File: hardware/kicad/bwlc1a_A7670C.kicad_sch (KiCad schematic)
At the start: 58 parts, among them J3 SIM_Card, J5 USB_BOOT, Q1 NPN, Q2 NPN, Q5 NPN, Q6 NPN, U5 MIC29302WU

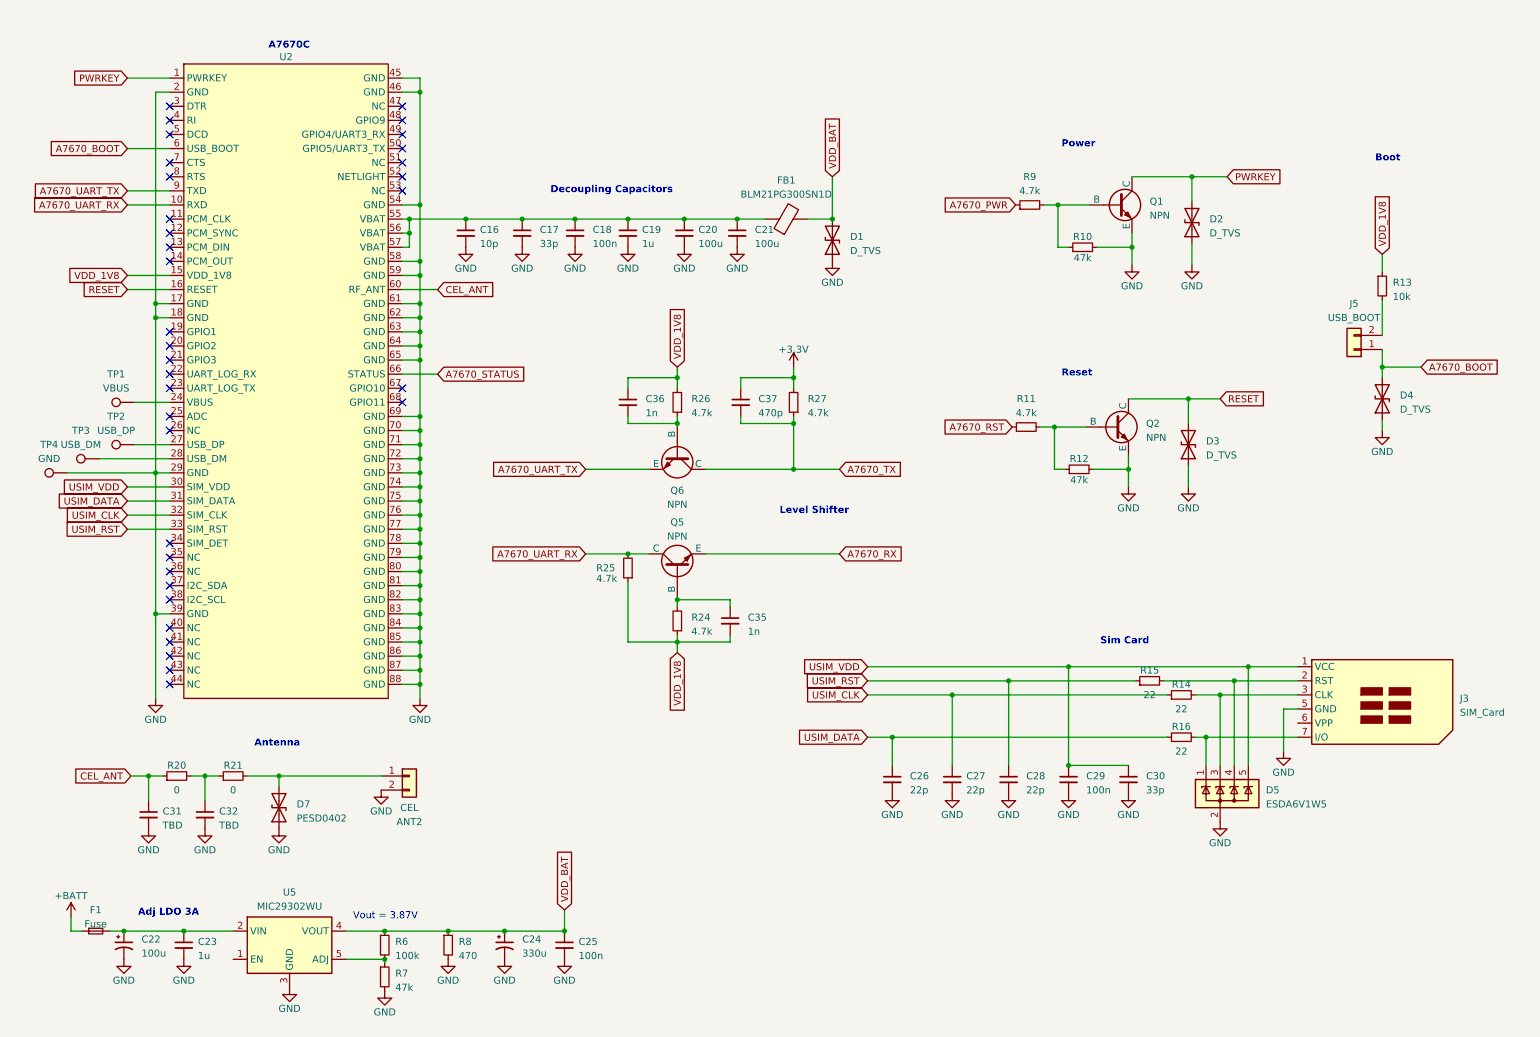
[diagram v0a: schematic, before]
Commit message: Finish Sch, start Layouting
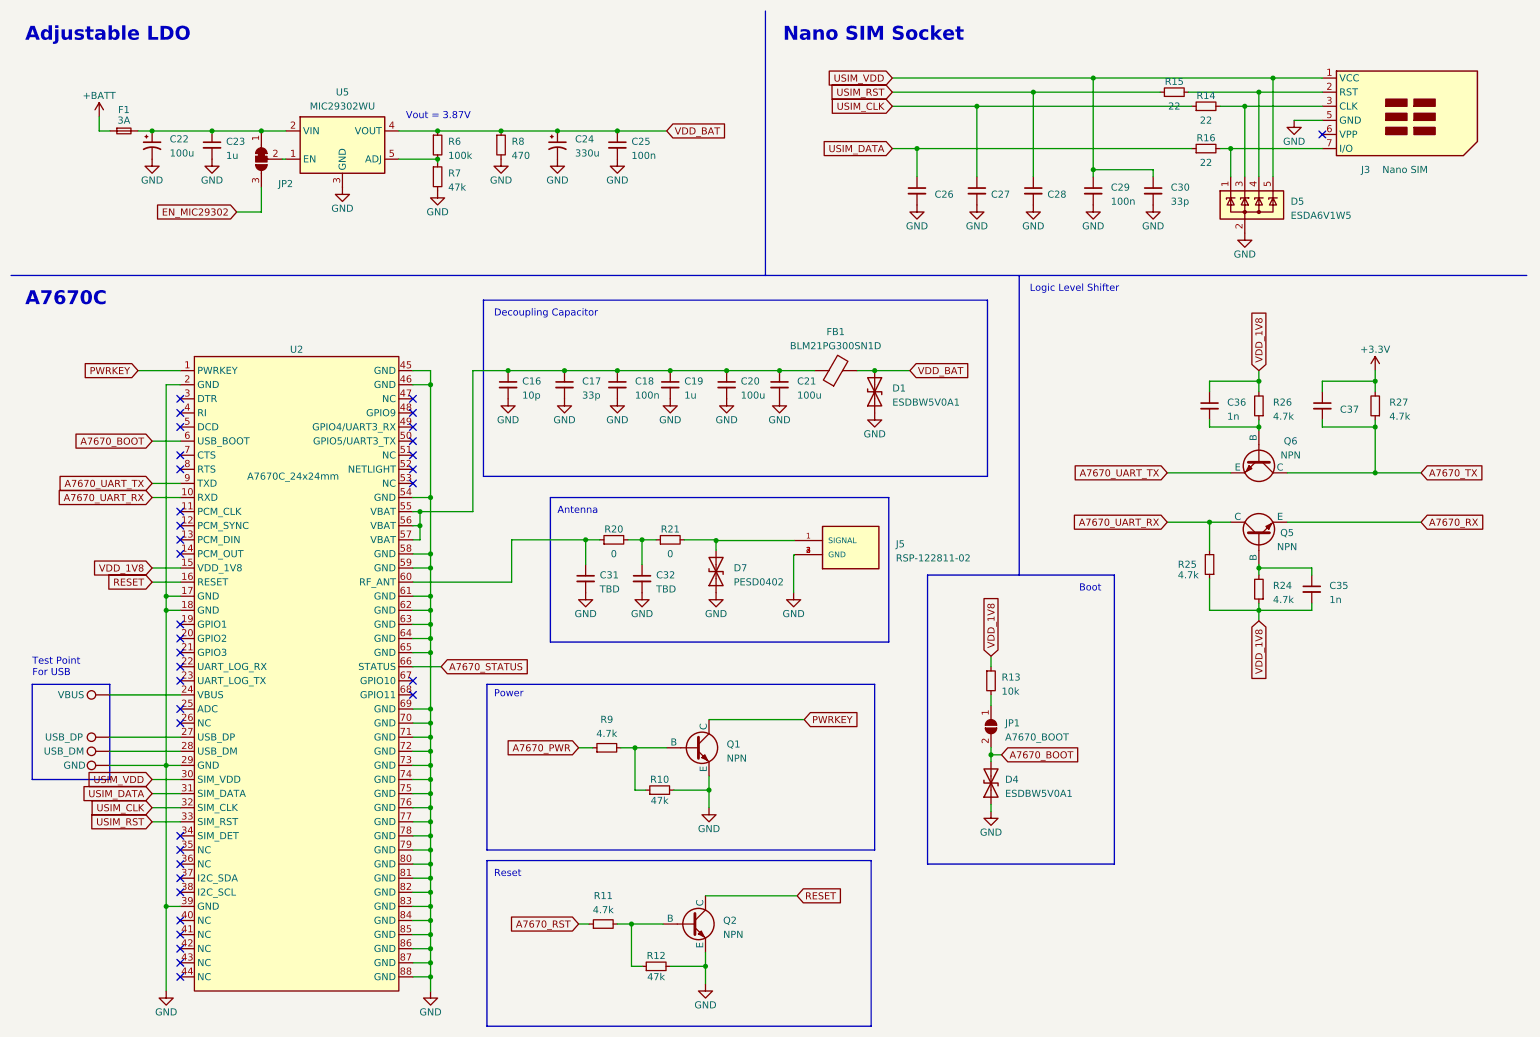
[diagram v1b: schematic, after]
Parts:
- removed ANT2: CEL, symbol Connector_Generic:Conn_01x02
- removed D2, D3: D_TVS, symbol Device:D_TVS
- removed J5: USB_BOOT, symbol Connector_Generic:Conn_01x02
- added J5: RSP-122811-02, SAMTEC_RSP-122811-02:SAMTEC_RSP-122811-02, symbol RSP-122811-02:RSP-122811-02
- added JP1: A7670_BOOT, Jumper:SolderJumper-2_P1.3mm_Open_RoundedPad1.0x1.5mm, symbol Jumper:SolderJumper_2_Open
- added JP2: EN_MIC29302, Jumper:SolderJumper-3_P1.3mm_Bridged2Bar12_RoundedPad1.0x1.5mm, symbol Jumper:SolderJumper_3_Bridged12
- C16, C17, C18, C19, C20, C21, C23, C25, C29, C30, C31, C32, C35, C36, D7: footprint (none) -> Capacitor_SMD:C_0402_1005Metric
- C22: footprint (none) -> Capacitor_SMD:CP_Elec_6.3x5.4
- C24: footprint (none) -> Capacitor_SMD:CP_Elec_8x10.5
- C26, C27, C28: value 22p -> 22p (N.C.); footprint (none) -> Capacitor_SMD:C_0402_1005Metric
- C37: value 470p -> 470p (N.C); footprint (none) -> Capacitor_SMD:C_0402_1005Metric
- D1, D4: value D_TVS -> ESDBW5V0A1; footprint (none) -> Capacitor_SMD:C_0402_1005Metric
- F1: value Fuse -> 3A; footprint (none) -> Fuse:Fuse_1206_3216Metric
- FB1: footprint (none) -> Capacitor_SMD:C_0805_2012Metric
- J3: value SIM_Card -> Nano SIM; footprint (none) -> GCT_SIM8051-6-0-14-00-X-REVD:GCT_SIM8051-6-0-14-00-X-REVD; Field4 (none) -> C266889
- Q1, Q2, Q5, Q6: footprint (none) -> Package_TO_SOT_SMD:SOT-23
- R10, R11, R12, R13, R14, R15, R16, R20, R21, R24, R25, R26, R27, R6, R7, R8, R9: footprint (none) -> Resistor_SMD:R_0402_1005Metric
- TP1, TP2, TP3, TP4: footprint (none) -> TestPoint:TestPoint_Pad_D1.5mm
- U2: value ~ -> A7670C_24x24mm; footprint (none) -> Teapot:A7670C_24x24mm
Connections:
- net A7670_BOOT: now also JP1.2 (B)
- net GND: now also J5.2 (GND), J5.3 (GND), J5.4 (GND)
- net at D7.2 (A2), R21.2: now also J5.1 (SIGNAL)
- net at R13.2: now also JP1.1 (A)
- net at C22.1, C23.1, F1.2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: now also JP2.1 (A)
- net at U5.1 (EN): now also JP2.2 (C)
- net CEL_ANT: no longer names the net of C31.1, R20.1, U2.60 (RF_ANT)
- new net EN_MIC29302: JP2.3 (B)
- no-connect marks 35 -> 36
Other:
- note added: "Adjustable LDO"
- note added: "Decoupling Capacitor"
- note added: "Logic Level Shifter"
- note added: "Nano SIM Socket"
- note added: "Test Point For USB"
- note removed: "Adj LDO 3A"
- note removed: "Decoupling Capacitors"
- note removed: "Level Shifter"
- note removed: "Sim Card"
- moved on the sheet: C16, C17, C18, C19, C20, C21, C22, C23, C24, C25, C26, C27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

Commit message: Update on PCB Layout
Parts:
- added C36: 100n, Capacitor_SMD:C_0402_1005Metric, symbol Device:C_Small
- C20, C21, C23: footprint Capacitor_SMD:C_0402_1005Metric -> Capacitor_SMD:C_0603_1608Metric
- C25: footprint Capacitor_SMD:C_0402_1005Metric -> Capacitor_SMD:C_0805_2012Metric
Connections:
- net GND: now also C36.2
- net VDD_1V8: now also C36.1
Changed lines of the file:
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@@
   (junction (at 139.065 107.442) (diameter 0) (color 0 0 0 0)
   )
+  (junction (at 27.305 112.395) (diameter 0) (color 0 0 0 0)
+  )
   (junction (at 40.005 173.355) (diameter 0) (color 0 0 0 0)
   )
@@
     (stroke (width 0) (type default))
   )
-  (wire (pts (xy 37.465 112.395) (xy 42.545 112.395))
+  (wire (pts (xy 26.035 112.395) (xy 27.305 112.395))
     (stroke (width 0) (type default))
   )
@@
     (stroke (width 0) (type default))
   )
+  (wire (pts (xy 27.305 112.395) (xy 42.545 112.395))
+    (stroke (width 0) (type default))
+  )
   (wire (pts (xy 87.63 109.855) (xy 87.63 99.695))
     (stroke (width 0) (type default))
@@
     )
   )
-  (global_label "VDD_1V8" (shape input) (at 37.465 112.395 180) (fields_autoplaced)
+  (global_label "VDD_1V8" (shape input) (at 26.035 112.395 180) (fields_autoplaced)
     (effects (font (size 1.27 1.27)) (justify right))
-    (property "Intersheetrefs" "${INTERSHEET_REFS}" (at 26.4554 112.395 0)
+    (property "Intersheetrefs" "${INTERSHEET_REFS}" (at 15.0254 112.395 0)
       (effects (font (size 1.27 1.27)) (justify right) hide)
     )
@@
       (effects (font (size 1.27 1.27)) (justify left))
     )
-    (property "Footprint" "Capacitor_SMD:C_0402_1005Metric" (at 140.97 79.375 0)
+    (property "Footprint" "Capacitor_SMD:C_0603_1608Metric" (at 140.97 79.375 0)
       (effects (font (size 1.27 1.27)) hide)
     )
@@
       (effects (font (size 1.27 1.27)) (justify left))
     )
-    (property "Footprint" "Capacitor_SMD:C_0402_1005Metric" (at 48.26 36.195 0)
+    (property "Footprint" "Capacitor_SMD:C_0603_1608Metric" (at 48.26 36.195 0)
       (effects (font (size 1.27 1.27)) hide)
     )
@@
       (effects (font (size 1.27 1.27)) (justify left))
     )
-    (property "Footprint" "Capacitor_SMD:C_0402_1005Metric" (at 121.285 36.195 0)
+    (property "Footprint" "Capacitor_SMD:C_0805_2012Metric" (at 121.285 36.195 0)
       (effects (font (size 1.27 1.27)) hide)
     )
@@
       (effects (font (size 1.27 1.27)) (justify left))
     )
-    (property "Footprint" "Capacitor_SMD:C_0402_1005Metric" (at 150.495 79.375 0)
+    (property "Footprint" "Capacitor_SMD:C_0603_1608Metric" (at 150.495 79.375 0)
       (effects (font (size 1.27 1.27)) hide)
     )
@@
     )
   )
+  (symbol (lib_id "Device:C_Small") (at 27.305 114.935 0) (unit 1)
+    (in_bom yes) (on_board yes) (dnp no) (fields_autoplaced)
+    (property "Reference" "C36" (at 30.48 114.3063 0)
+      (effects (font (size 1.27 1.27)) (justify left))
+    )
+    (property "Value" "100n" (at 30.48 116.8463 0)
+      (effects (font (size 1.27 1.27)) (justify left))
+    )
+    (property "Footprint" "Capacitor_SMD:C_0402_1005Metric" (at 27.305 114.935 0)
+      (effects (font (size 1.27 1.27)) hide)
+    )
+    (property "Datasheet" "~" (at 27.305 114.935 0)
+      (effects (font (size 1.27 1.27)) hide)
+    )
+    (pin "1")
+    (pin "2")
+    (instances
+      (project "bwlc1a"
+        (path "/388039b1-99cc-430f-bd4a-010573fde798"
+          (reference "C36") (unit 1)
+        )
+        (path "/388039b1-99cc-430f-bd4a-010573fde798/d0b0fe7e-ffcb-4a20-b7b5-70f0caeaf6a1"
+          (reference "C38") (unit 1)
+        )
+      )
+    )
+  )
   (symbol (lib_id "power:GND") (at 115.57 116.84 0) (unit 1)
     (in_bom yes) (on_board yes) (dnp no)
@@
         )
       )
+    )
+  )
+  (symbol (lib_id "power:GND") (at 27.305 117.475 0) (unit 1)
+    (in_bom yes) (on_board yes) (dnp no)
+    (property "Reference" "#PWR063" (at 27.305 123.825 0)
+      (effects (font (size 1.27 1.27)) hide)
+    )
+    (property "Value" "GND" (at 27.305 121.285 0)
+      (effects (font (size 1.27 1.27)))
+    )
+    (property "Footprint" "" (at 27.305 117.475 0)
+      (effects (font (size 1.27 1.27)) hide)
+    )
+    (property "Datasheet" "" (at 27.305 117.475 0)
+      (effects (font (size 1.27 1.27)) hide)
+    )
+    (pin "1")
+    (instances
+      (project "bwlc1a"
+        (path "/388039b1-99cc-430f-bd4a-010573fde798"
+          (reference "#PWR063") (unit 1)
+        )
+        (path "/388039b1-99cc-430f-bd4a-010573fde798/d0b0fe7e-ffcb-4a20-b7b5-70f0caeaf6a1"
+          (reference "#PWR089") (unit 1)
+        )
+      )

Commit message: Update on routing
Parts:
- removed C26, C27, C28: 22p (N.C.), Capacitor_SMD:C_0402_1005Metric, symbol Device:C_Small
- removed C30: 33p, Capacitor_SMD:C_0402_1005Metric, symbol Device:C_Small
- C24: footprint Capacitor_SMD:CP_Elec_8x10.5 -> Capacitor_SMD:CP_Elec_6.3x7.7

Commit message: PCB Layout update + Silkscreen
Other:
- moved on the sheet: JP2
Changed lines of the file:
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@@
   (junction (at 88.9 38.735) (diameter 0) (color 0 0 0 0)
   )
+  (junction (at 57.785 33.655) (diameter 0) (color 0 0 0 0)
+  )
   (junction (at 87.63 155.575) (diameter 0) (color 0 0 0 0)
   )
@@
   )
   (junction (at 87.63 163.195) (diameter 0) (color 0 0 0 0)
-  )
-  (junction (at 57.15 33.655) (diameter 0) (color 0 0 0 0)
   )
   (junction (at 40.005 120.015) (diameter 0) (color 0 0 0 0)
@@
     (stroke (width 0) (type default))
   )
-  (wire (pts (xy 48.26 33.655) (xy 57.15 33.655))
-    (stroke (width 0) (type default))
-  )
   (wire (pts (xy 84.455 145.415) (xy 87.63 145.415))
     (stroke (width 0) (type default))
@@
     (stroke (width 0) (type default))
   )
+  (wire (pts (xy 57.785 48.26) (xy 49.53 48.26))
+    (stroke (width 0) (type default))
+  )
   (wire (pts (xy 87.63 153.035) (xy 87.63 150.495))
     (stroke (width 0) (type default))
@@
     (stroke (width 0) (type default))
   )
+  (wire (pts (xy 57.785 33.655) (xy 61.595 33.655))
+    (stroke (width 0) (type default))
+  )
   (wire (pts (xy 84.455 168.275) (xy 87.63 168.275))
     (stroke (width 0) (type default))
@@
     (stroke (width 0) (type default))
   )
-  (wire (pts (xy 57.15 48.26) (xy 57.15 43.815))
-    (stroke (width 0) (type default))
-  )
   (wire (pts (xy 37.465 89.535) (xy 42.545 89.535))
     (stroke (width 0) (type default))
@@
     (stroke (width 0) (type default))
   )
-  (wire (pts (xy 57.15 33.655) (xy 61.595 33.655))
+  (wire (pts (xy 48.26 33.655) (xy 57.785 33.655))
     (stroke (width 0) (type default))
   )
@@
     (stroke (width 0) (type default))
   )
+  (wire (pts (xy 57.785 43.815) (xy 57.785 48.26))
+    (stroke (width 0) (type default))
+  )
   (wire (pts (xy 84.455 104.775) (xy 85.725 104.775))
     (stroke (width 0) (type default))
@@
     (stroke (width 0) (type default))
   )
-  (wire (pts (xy 52.705 48.26) (xy 57.15 48.26))
-    (stroke (width 0) (type default))
-  )
   (wire (pts (xy 40.005 117.475) (xy 40.005 79.375))
     (stroke (width 0) (type default))
@@
   )
   (wire (pts (xy 84.455 155.575) (xy 87.63 155.575))
-    (stroke (width 0) (type default))
-  )
-  (wire (pts (xy 60.96 38.735) (xy 61.595 38.735))
     (stroke (width 0) (type default))
   )
@@
     )
   )
-  (global_label "EN_MIC29302" (shape input) (at 52.705 48.26 180) (fields_autoplaced)
+  (global_label "EN_MIC29302" (shape input) (at 49.53 48.26 180) (fields_autoplaced)
     (effects (font (size 1.27 1.27)) (justify right))
-    (property "Intersheetrefs" "${INTERSHEET_REFS}" (at 36.9784 48.26 0)
+    (property "Intersheetrefs" "${INTERSHEET_REFS}" (at 33.8034 48.26 0)
       (effects (font (size 1.27 1.27)) (justify right) hide)
     )
@@
   )
   (symbol (lib_id "Device:C_Small") (at 27.305 114.935 0) (unit 1)
-    (in_bom yes) (on_board yes) (dnp no) (fields_autoplaced)
-    (property "Reference" "C36" (at 30.48 114.3063 0)
-      (effects (font (size 1.27 1.27)) (justify left))
-    )
-    (property "Value" "100n" (at 30.48 116.8463 0)
+    (in_bom yes) (on_board yes) (dnp no)
+    (property "Reference" "C36" (at 20.955 114.935 0)
+      (effects (font (size 1.27 1.27)) (justify left))
+    )
+    (property "Value" "100n" (at 19.685 116.84 0)
       (effects (font (size 1.27 1.27)) (justify left))
     )
@@
     )
   )
-  (symbol (lib_id "Jumper:SolderJumper_3_Bridged12") (at 57.15 38.735 90) (mirror x) (unit 1)
-    (in_bom yes) (on_board yes) (dnp no)
-    (property "Reference" "JP2" (at 62.865 43.18 90)
-      (effects (font (size 1.27 1.27)) (justify left))
-    )
-    (property "Value" "EN_MIC29302" (at 72.39 45.085 90)
+  (symbol (lib_id "Jumper:SolderJumper_3_Bridged12") (at 57.785 38.735 90) (mirror x) (unit 1)
+    (in_bom yes) (on_board yes) (dnp no)
+    (property "Reference" "JP2" (at 63.5 43.18 90)
+      (effects (font (size 1.27 1.27)) (justify left))
+    )
+    (property "Value" "EN_MIC29302" (at 73.025 45.085 90)
       (effects (font (size 1.27 1.27)) (justify left) hide)
     )
-    (property "Footprint" "Jumper:SolderJumper-3_P1.3mm_Bridged2Bar12_RoundedPad1.0x1.5mm" (at 57.15 38.735 0)
-      (effects (font (size 1.27 1.27)) hide)
-    )
-    (property "Datasheet" "~" (at 57.15 38.735 0)
-      (effects (font (size 1.27 1.27)) hide)
-    )
+    (property "Footprint" "Jumper:SolderJumper-3_P1.3mm_Bridged2Bar12_RoundedPad1.0x1.5mm" (at 57.785 38.735 0)
+      (effects (font (size 1.27 1.27)) hide)
+    )
+    (property "Datasheet" "~" (at 57.785 38.735 0)
+      (effects (font (size 1.27 1.27)) hide)
+    )
